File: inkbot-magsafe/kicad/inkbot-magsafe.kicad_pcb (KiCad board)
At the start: 4 copper layers, 60 x 99 mm, 0 parts

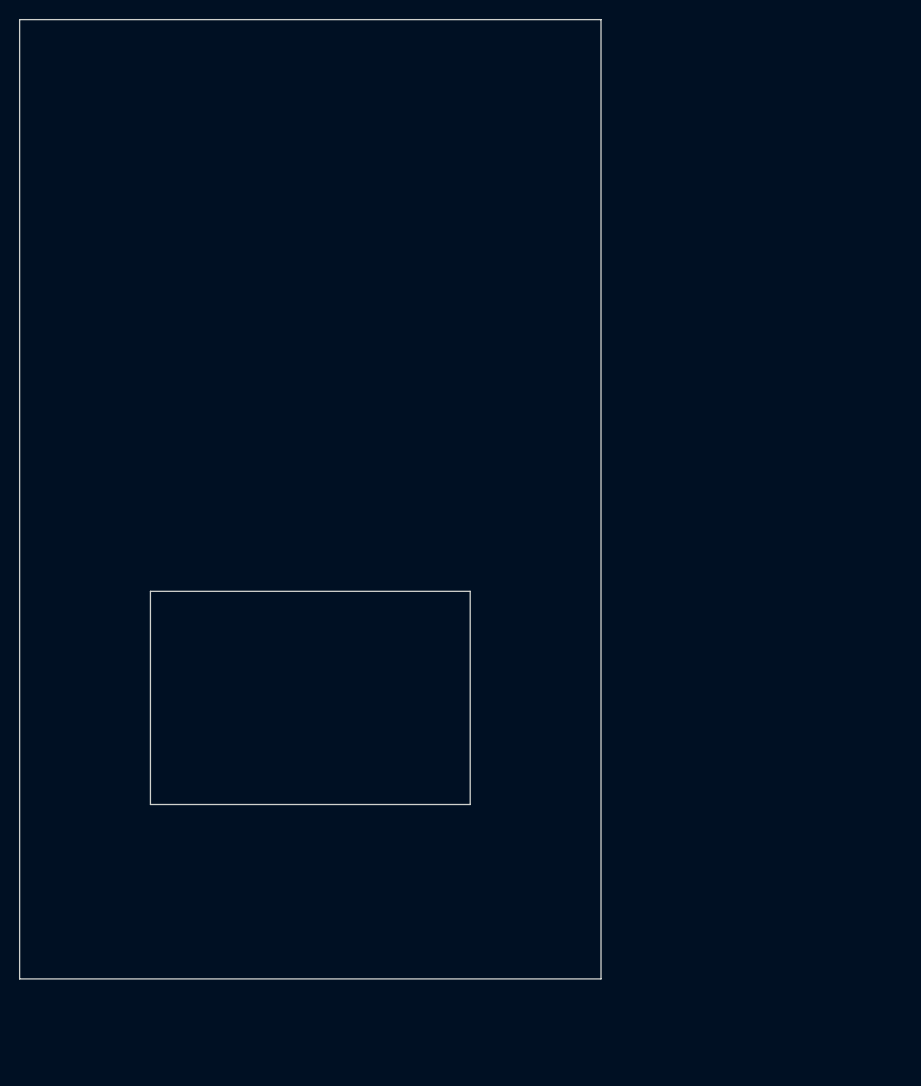
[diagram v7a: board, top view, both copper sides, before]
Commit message: inkbot-magsafe: harden the EVT hardware design
Co-authored-by: Jason Hall <imjasonh@users.noreply.github.com>
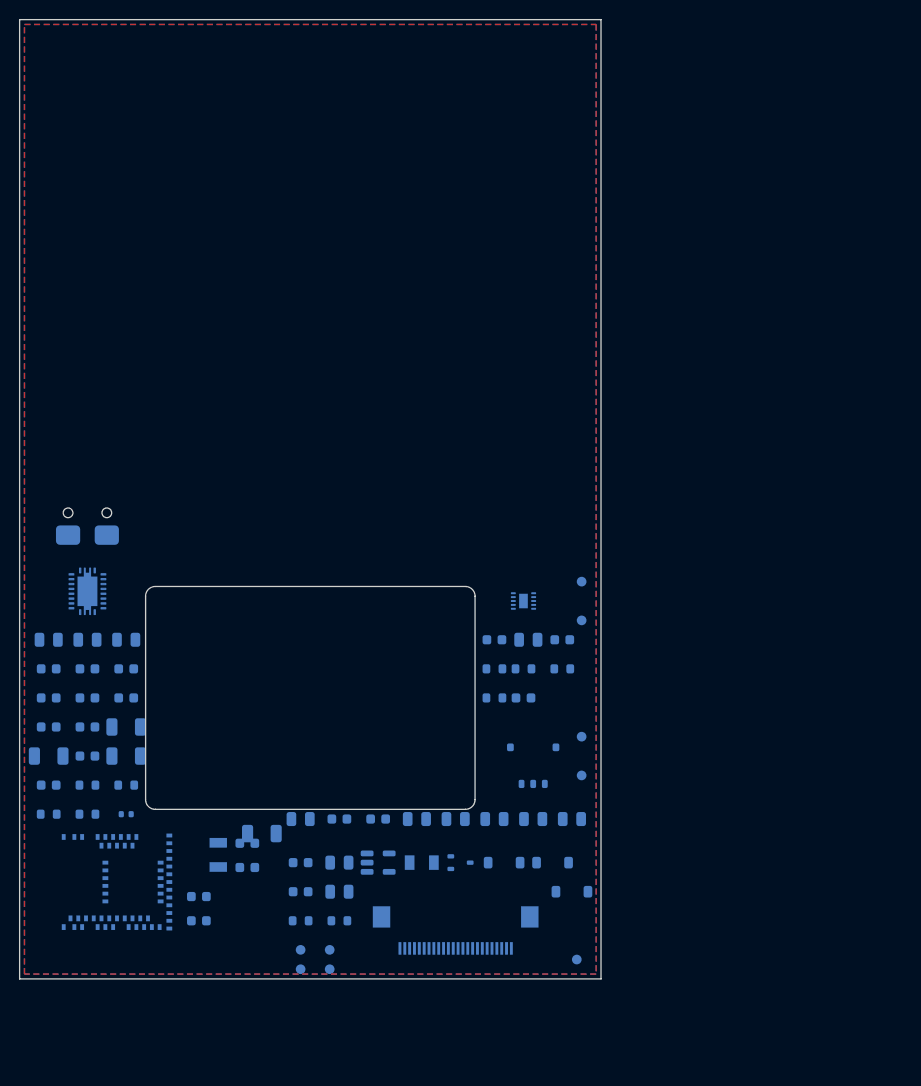
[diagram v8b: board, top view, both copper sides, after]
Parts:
- added C1: C_0805_2012Metric, Capacitor_SMD:C_0805_2012Metric, B.Cu at (3.00, 64.0)
- added C10: C_0603_1608Metric, Capacitor_SMD:C_0603_1608Metric, B.Cu at (3.00, 73.0)
- added C11: C_0603_1608Metric, Capacitor_SMD:C_0603_1608Metric, B.Cu at (7.00, 73.0)
- added C12: C_1206_3216Metric, Capacitor_SMD:C_1206_3216Metric, B.Cu at (11.0, 73.0)
- added C13: C_1206_3216Metric, Capacitor_SMD:C_1206_3216Metric, B.Cu at (3.00, 76.0)
- added C14: C_0603_1608Metric, Capacitor_SMD:C_0603_1608Metric, B.Cu at (7.00, 76.0)
- added C15: C_1206_3216Metric, Capacitor_SMD:C_1206_3216Metric, B.Cu at (11.0, 76.0)
- added C16: C_0603_1608Metric, Capacitor_SMD:C_0603_1608Metric, B.Cu at (3.00, 79.0)
- added C17: C_0603_1608Metric, Capacitor_SMD:C_0603_1608Metric, B.Cu at (49.0, 64.0)
- added C18: C_0805_2012Metric, Capacitor_SMD:C_0805_2012Metric, B.Cu at (52.5, 64.0)
- added C19: C_0603_1608Metric, Capacitor_SMD:C_0603_1608Metric, B.Cu at (56.0, 64.0)
- added C2: C_0805_2012Metric, Capacitor_SMD:C_0805_2012Metric, B.Cu at (7.00, 64.0)
- added C20: C_0603_1608Metric, Capacitor_SMD:C_0603_1608Metric, B.Cu at (52.0, 70.0)
- added C21: C_0603_1608Metric, Capacitor_SMD:C_0603_1608Metric, B.Cu at (18.5, 90.5)
- added C22: C_0603_1608Metric, Capacitor_SMD:C_0603_1608Metric, B.Cu at (18.5, 93.0)
- added C23: C_0603_1608Metric, Capacitor_SMD:C_0603_1608Metric, B.Cu at (23.5, 85.0)
- added C24: C_0603_1608Metric, Capacitor_SMD:C_0603_1608Metric, B.Cu at (23.5, 87.5)
- added C26: C_0603_1608Metric, Capacitor_SMD:C_0603_1608Metric, B.Cu at (29.0, 87.0)
- added C27: C_0805_2012Metric, Capacitor_SMD:C_0805_2012Metric, B.Cu at (33.0, 87.0)
- added C28: C_0805_2012Metric, Capacitor_SMD:C_0805_2012Metric, B.Cu at (29.0, 82.5)
- added C29: C_0603_1608Metric, Capacitor_SMD:C_0603_1608Metric, B.Cu at (33.0, 82.5)
- added C3: C_0805_2012Metric, Capacitor_SMD:C_0805_2012Metric, B.Cu at (11.0, 64.0)
- added C30: C_0603_1608Metric, Capacitor_SMD:C_0603_1608Metric, B.Cu at (37.0, 82.5)
- added C31: C_0805_2012Metric, Capacitor_SMD:C_0805_2012Metric, B.Cu at (41.0, 82.5)
- added C32: C_0805_2012Metric, Capacitor_SMD:C_0805_2012Metric, B.Cu at (45.0, 82.5)
- added C33: C_0805_2012Metric, Capacitor_SMD:C_0805_2012Metric, B.Cu at (49.0, 82.5)
- added C34: C_0805_2012Metric, Capacitor_SMD:C_0805_2012Metric, B.Cu at (53.0, 82.5)
- added C35: C_0805_2012Metric, Capacitor_SMD:C_0805_2012Metric, B.Cu at (57.0, 82.5)
- added C36: C_0603_1608Metric, Capacitor_SMD:C_0603_1608Metric, B.Cu at (29.0, 90.0)
- added C37: C_0805_2012Metric, Capacitor_SMD:C_0805_2012Metric, B.Cu at (33.0, 90.0)
- added C38: C_1206_3216Metric, Capacitor_SMD:C_1206_3216Metric, B.Cu at (25.0, 84.0)
- added C4: C_0603_1608Metric, Capacitor_SMD:C_0603_1608Metric, B.Cu at (3.00, 67.0)
- added C5: C_0603_1608Metric, Capacitor_SMD:C_0603_1608Metric, B.Cu at (7.00, 67.0)
- added C6: C_0603_1608Metric, Capacitor_SMD:C_0603_1608Metric, B.Cu at (11.0, 67.0)
- added C7: C_0603_1608Metric, Capacitor_SMD:C_0603_1608Metric, B.Cu at (3.00, 70.0)
- added C8: C_0603_1608Metric, Capacitor_SMD:C_0603_1608Metric, B.Cu at (7.00, 70.0)
- added C9: C_0603_1608Metric, Capacitor_SMD:C_0603_1608Metric, B.Cu at (11.0, 70.0)
- added D1: D_SOD-123, Diode_SMD:D_SOD-123, B.Cu at (57.0, 90.0)
- added D2: D_SOD-123, Diode_SMD:D_SOD-123, B.Cu at (55.0, 87.0)
- added D3: D_SOD-123, Diode_SMD:D_SOD-123, B.Cu at (50.0, 87.0)
- added J1: Hirose_FH12-24S-0.5SH_1x24-1MP_P0.50mm_Horizontal, Connector_FFC-FPC:Hirose_FH12-24S-0.5SH_1x24-1MP_P0.50mm_Horizontal, B.Cu at (45.0, 94.0)
- added J2: Molex_Pico-EZmate_78171-0003_1x03-1MP_P1.20mm_Vertical, Connector_Molex:Molex_Pico-EZmate_78171-0003_1x03-1MP_P1.20mm_Vertical, B.Cu at (53.0, 77.0)
- added J3: Coil_SolderPads, inkbot_magsafe:Coil_SolderPads, B.Cu at (7.00, 52.5)
- added L1: L_TDK_NLV25_2.5x2.0mm, Inductor_SMD:L_TDK_NLV25_2.5x2.0mm, B.Cu at (41.5, 87.0)
- added Q1: SOT-323_SC-70, Package_TO_SOT_SMD:SOT-323_SC-70, B.Cu at (45.5, 87.0)
- added R1: R_0603_1608Metric, Resistor_SMD:R_0603_1608Metric, B.Cu at (7.00, 79.0)
- added R11: R_0603_1608Metric, Resistor_SMD:R_0603_1608Metric, B.Cu at (29.0, 93.0)
- added R12: R_0603_1608Metric, Resistor_SMD:R_0603_1608Metric, B.Cu at (33.0, 93.0)
- added R2: R_0603_1608Metric, Resistor_SMD:R_0603_1608Metric, B.Cu at (11.0, 79.0)
- added R3: R_0603_1608Metric, Resistor_SMD:R_0603_1608Metric, B.Cu at (3.00, 82.0)
- added R4: R_0603_1608Metric, Resistor_SMD:R_0603_1608Metric, B.Cu at (7.00, 82.0)
- added R5: R_0603_1608Metric, Resistor_SMD:R_0603_1608Metric, B.Cu at (49.0, 67.0)
- added R6: R_0603_1608Metric, Resistor_SMD:R_0603_1608Metric, B.Cu at (52.0, 67.0)
- added R7: R_0603_1608Metric, Resistor_SMD:R_0603_1608Metric, B.Cu at (56.0, 67.0)
- added R8: R_0603_1608Metric, Resistor_SMD:R_0603_1608Metric, B.Cu at (49.0, 70.0)
- added RT2: R_0402_1005Metric, Resistor_SMD:R_0402_1005Metric, B.Cu at (11.0, 82.0)
- added TP1: TestPoint_Pad_D1.0mm, TestPoint:TestPoint_Pad_D1.0mm, B.Cu at (29.0, 96.0)
- added TP2: TestPoint_Pad_D1.0mm, TestPoint:TestPoint_Pad_D1.0mm, B.Cu at (32.0, 96.0)
- added TP3: TestPoint_Pad_D1.0mm, TestPoint:TestPoint_Pad_D1.0mm, B.Cu at (29.0, 98.0)
- added TP4: TestPoint_Pad_D1.0mm, TestPoint:TestPoint_Pad_D1.0mm, B.Cu at (32.0, 98.0)
- added TP5: TestPoint_Pad_D1.0mm, TestPoint:TestPoint_Pad_D1.0mm, B.Cu at (57.5, 97.0)
- added TP6: TestPoint_Pad_D1.0mm, TestPoint:TestPoint_Pad_D1.0mm, B.Cu at (58.0, 58.0)
- added TP7: TestPoint_Pad_D1.0mm, TestPoint:TestPoint_Pad_D1.0mm, B.Cu at (58.0, 62.0)
- added TP8: TestPoint_Pad_D1.0mm, TestPoint:TestPoint_Pad_D1.0mm, B.Cu at (58.0, 74.0)
- added TP9: TestPoint_Pad_D1.0mm, TestPoint:TestPoint_Pad_D1.0mm, B.Cu at (58.0, 78.0)
- added U1: Raytac_MDBT50Q, RF_Module:Raytac_MDBT50Q, B.Cu at (8.30, 89.0)
- added U2: Texas_VQFN-RHL-20, Package_DFN_QFN:Texas_VQFN-RHL-20, B.Cu at (7.00, 59.0)
- added U3: BQ25185_DLH0010A, inkbot_magsafe:BQ25185_DLH0010A, B.Cu at (52.0, 60.0)
- added U4: SOT-23-5, Package_TO_SOT_SMD:SOT-23-5, B.Cu at (37.0, 87.0)
- added Y1: Crystal_SMD_3215-2Pin_3.2x1.5mm, Crystal:Crystal_SMD_3215-2Pin_3.2x1.5mm, B.Cu at (20.5, 86.2)
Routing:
- added copper zone on In1.Cu, net /SYS
- added copper zone on B.Cu, net GND
- added copper zone on F.Cu, net GND
- added copper zone on In2.Cu, net GND
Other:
- outline, holes or cut-outs redrawn
- board text added: "orientation magnet"
